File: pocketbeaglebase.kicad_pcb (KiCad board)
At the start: 2 copper layers, 100 x 60 mm, 87 parts, among them J1 RJ45-TRANSFO-2, P1 USB_2.0_Connector, P2 DSUB-9, P3 CONN_01X04, P4 CONN_02X20, P5 CONN_01X04, P6 CONN_01X04, P7 CONN_01X04, P8 CONN_02X03, P9 WR-TBL_691322310002, U1 BEAGLE_PocketBeagle, U2 LAN9514, U3 MIC2026, U4 MAX3227, U5 93LC66, U6 TPS54335A, Y1 25MHz

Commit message: review and discussion done
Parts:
- added P10: CONN_01X03, CON_wuerth:WR-TBL_691322310003, F.Cu at (181.9, 59.1)
- added U7: SN65HVD232, SOIC:SOIJ-8_5.3x5.3mm_Pitch1.27mm, F.Cu at (167.1, 34.1)
- C22, C24, C26, C27, C28: footprint capacitors:TantalC_SizeS_EIA-3216 -> capacitors:C_0603
- P2: value DSUB-9 -> CONN_01X03; footprint mechanical-connectors:DSUB-9_Female_Horizontal_P2.77x2.84mm_EdgePinOffset7.70mm_Housed_MountingHolesOffset9.12mm -> CON_wuerth:WR-TBL_691322310003
- moved P2 13.2 mm to (181.9, 74.0)
- moved C1 1.66 mm to (150.7, 80.5)
- moved C22 1.59 mm to (104.3, 62.8), turned to 270 degrees
- moved Y1 1.06 mm to (154.9, 80.0)
- moved C2 0.96 mm to (159.8, 80.0)
- moved C27 0.89 mm to (109.2, 60.1), turned to 0 degrees
- moved R2 0.75 mm to (155.6, 76.0)
- moved C28 0.64 mm to (109.8, 69.9), turned to 0 degrees
- moved C24 0.59 mm to (116.3, 64.6), turned to 90 degrees
- moved C26 0.56 mm to (104.3, 66.2), turned to 270 degrees
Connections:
- P2 pad 1: (no net) -> Net-(P2-Pad1)
- P2 pad 3: Net-(P2-Pad3) -> GND
- P4 pad 29: SCL2 -> (no net)
- P4 pad 31: SDA2 -> (no net)
- R21 pad 2: SDA2 -> (no net)
- R22 pad 2: SCL2 -> (no net)
- U1 pad 26: SDA2 -> (no net)
- U1 pad 28: SCL2 -> (no net)
- U4 pad 13: Net-(P2-Pad2) -> Net-(P2-Pad1)
- U4 pad 8: Net-(P2-Pad3) -> Net-(P2-Pad2)
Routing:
- net (no net): track 0.00 -> 108.8 mm, vias 0 -> 2
- net Net-(P2-Pad1): track 0.00 -> 87.4 mm, vias 0 -> 1
- net Net-(P2-Pad3): track 81.8 -> 0.00 mm, vias 1 -> 0
- net SDA2: track 56.2 -> 0.00 mm, vias 1 -> 0
- net SCL2: track 52.5 -> 0.00 mm, vias 1 -> 0
- net Net-(P2-Pad2): track 78.8 -> 91.3 mm
- net Net-(J1-Pad12): track 82.6 -> 87.1 mm
- net Net-(J1-Pad14): track 74.6 -> 79.0 mm
- net /LAN9514/nPWR2: track 56.6 -> 58.9 mm
- net Net-(C22-Pad1): track 5.05 -> 3.01 mm
- net GND: track 63.0 -> 64.4 mm, vias 16 -> 36
- net Net-(C1-Pad1): track 14.4 -> 15.7 mm
- net USB_DP: track 52.8 -> 51.6 mm
- net USB_DM: track 47.4 -> 46.2 mm
- net /LAN9514/nEEDO: track 10.8 -> 11.8 mm
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
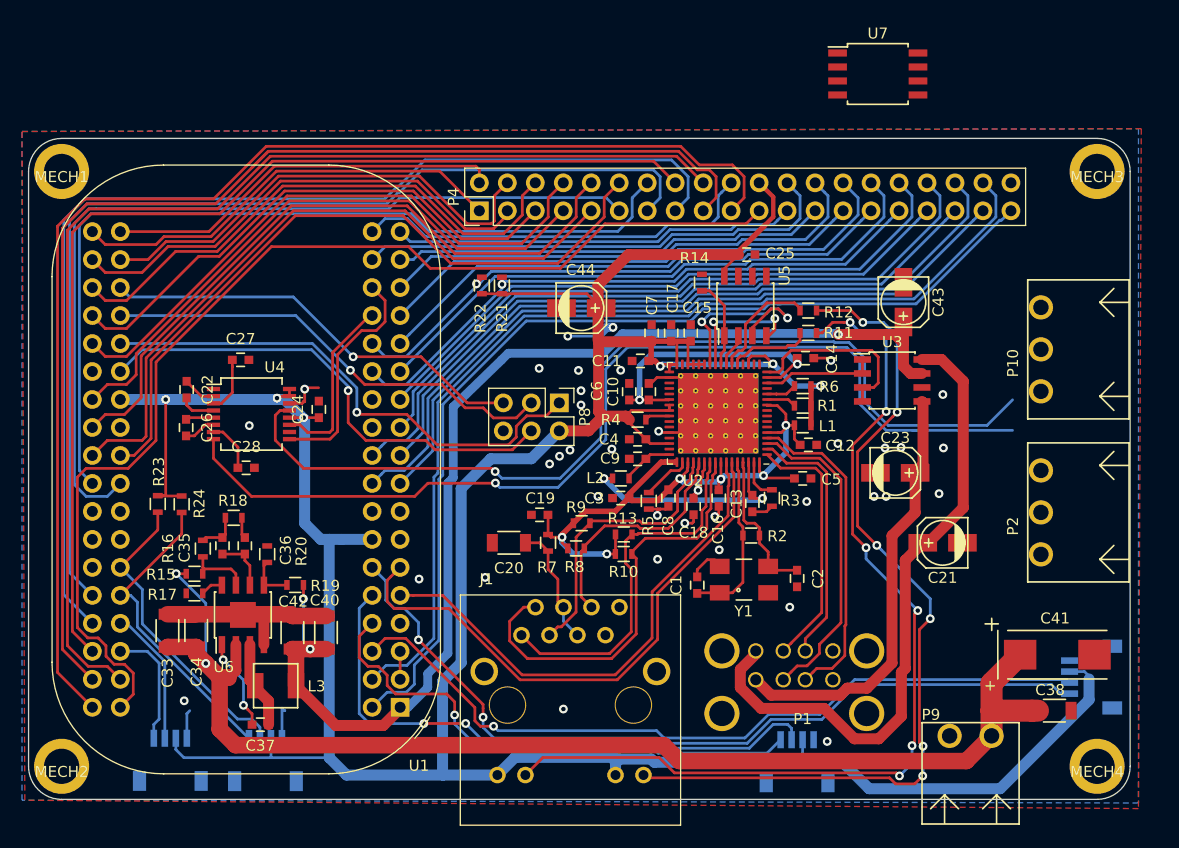
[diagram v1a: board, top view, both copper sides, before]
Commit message: added can bus
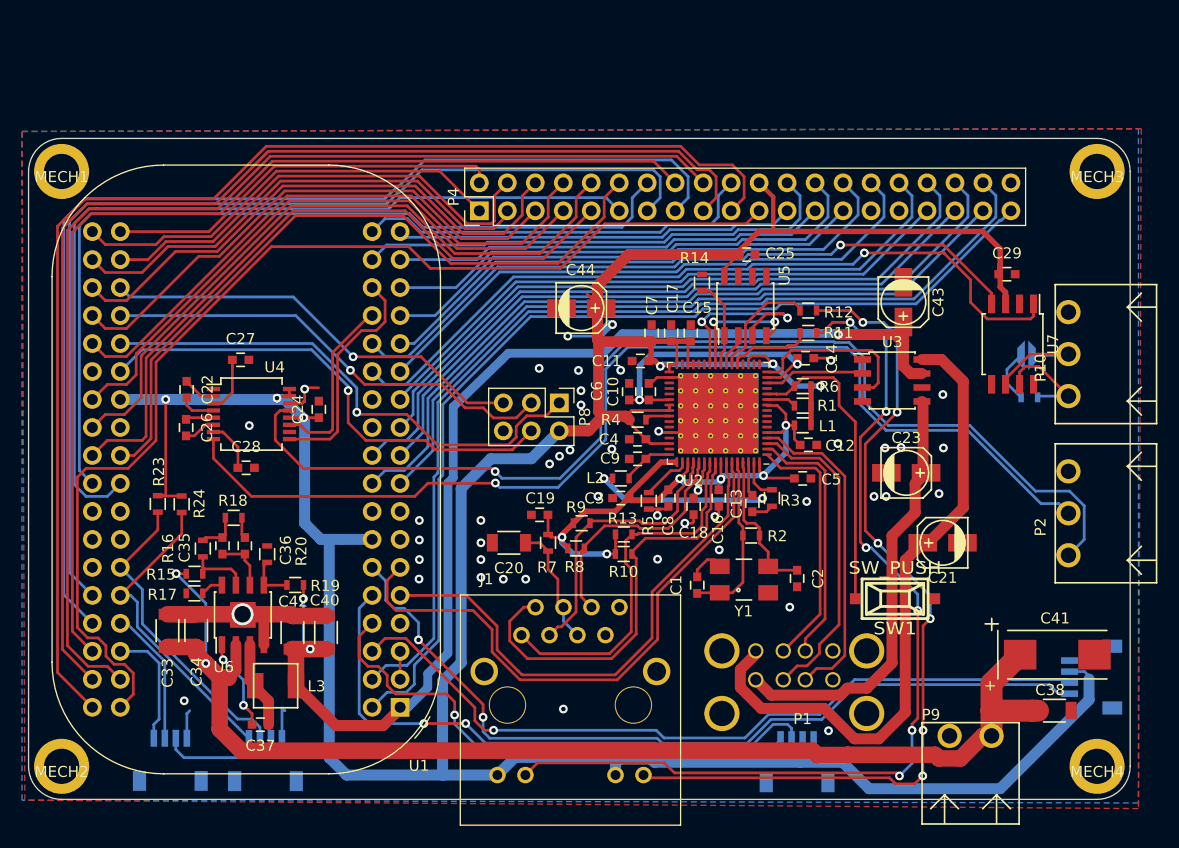
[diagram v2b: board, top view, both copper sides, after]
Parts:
- removed R22: 10k, resistors:R_0603
- added C29: 100nF, capacitors:C_0603, F.Cu at (178.8, 52.3)
- added P11: CONN_01X02, wire_pads:SolderJumper_2mm, B.Cu at (180.6, 59.7)
- added SW1: SW_PUSH, mechanical-switches:smd_push, F.Cu at (168.7, 81.8)
- P9: value WR-TBL_691322310002 -> WR-TBL_ 691322310002
- R21: value 10k -> 120R; moved to B.Cu
- moved R21 48.9 mm to (180.8, 63.5), turned to 0 degrees
- moved U7 27.4 mm to (179.3, 58.7), turned to 270 degrees
- moved P10 2.54 mm to (184.4, 59.6)
- moved P2 2.50 mm to (184.4, 74.0)
- moved C23 0.99 mm to (169.7, 70.4)
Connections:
- net Net-(P10-Pad2) renamed /UART/nCANL
- P10 pad 1: Net-(P10-Pad1) -> /UART/nCANH
- R21 pad 1: +3V3 -> Net-(P11-Pad1)
- R21 pad 2: (no net) -> /UART/nCANH
- U1 pad 26: (no net) -> CAN0_TX
- U1 pad 28: (no net) -> CAN0_RX
- U7 pad 1: (no net) -> CAN0_TX
- U7 pad 2: (no net) -> GND
- U7 pad 3: (no net) -> +3V3
- U7 pad 4: (no net) -> CAN0_RX
- U7 pad 7: Net-(P10-Pad1) -> /UART/nCANH
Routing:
- net (no net): track 108.8 -> 0.00 mm, vias 2 -> 0
- net CAN0_TX: track 0.00 -> 70.4 mm, vias 0 -> 1
- net CAN0_RX: track 0.00 -> 63.7 mm, vias 0 -> 1
- net Net-(R6-Pad1): track 2.79 -> 27.5 mm
- net +3V3: track 315.6 -> 333.8 mm
- net Net-(P2-Pad1): track 87.4 -> 101.0 mm
- net /UART/nCANL: track 0.00 -> 10.5 mm
- net /UART/nCANH: track 0.00 -> 9.71 mm
- net Net-(P2-Pad2): track 91.3 -> 99.4 mm
- net Net-(P11-Pad1): track 0.00 -> 4.88 mm
- net USB_DM: track 46.2 -> 47.5 mm
- net USB_DP: track 51.6 -> 52.8 mm
- net Net-(J1-Pad14): track 79.0 -> 78.1 mm
- net Net-(J1-Pad12): track 87.1 -> 86.4 mm
- net /LAN9514/nEEDI: track 18.0 -> 17.3 mm
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
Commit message: somehow done with general layouting
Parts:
- added D1: TVS, diodes:DO-214AB, F.Cu at (183.5, 86.7)
- P9: value WR-TBL_ 691322310002 -> WR-TBL_691322310002
- moved C38 77.4 mm to (105.7, 91.3), turned to 180 degrees
- moved C41 75.9 mm to (108.0, 95.9), turned to 180 degrees
- moved C21 5.40 mm to (177.0, 73.2)
- moved P6 2.29 mm to (186.4, 86.6)
- moved P7 1.91 mm to (113.4, 96.4)
- moved SW1 1.42 mm to (168.8, 80.4)
- moved P5 0.81 mm to (103.7, 96.4)
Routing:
- net GND: track 64.4 -> 85.2 mm, vias 45 -> 107
- net +BATT: track 110.0 -> 107.3 mm
- net +3V3: track 333.8 -> 331.2 mm
- net SCL1: track 28.2 -> 30.5 mm
- net Net-(J1-Pad14): track 78.1 -> 76.1 mm, vias 6 -> 4
- net SDA1: track 28.0 -> 29.9 mm
- net RX2: track 47.7 -> 46.0 mm
- net PR1_TX: track 70.6 -> 72.1 mm
- net Net-(R6-Pad1): track 27.5 -> 26.2 mm
- net Net-(J1-Pad12): track 86.4 -> 85.4 mm, vias 6 -> 4
- net PR1_RX: track 75.8 -> 76.6 mm

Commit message: finally
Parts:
- added L4: Label, labels:jecc_logo_7.2x2.2, F.Cu at (101.9, 43.4)
- added L5: Label, labels:Bot, F.Cu at (186.2, 48.5)
- added L6: Label, labels:Top, F.Cu at (186.2, 48.5)
- Y1: footprint crystals:Crystal_SMD_0603_4Pads -> crystals:Crystal_SMD_5x3.2mm_4Pad
- moved Y1 0.33 mm to (155.2, 80.3), turned to 180 degrees
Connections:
- U1 pad 3: USB_VBUS -> (no net)
- U1 pad 7: (no net) -> USB_VBUS
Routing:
- net GND: track 85.2 -> 145.7 mm, vias 107 -> 135
- net +3V3: track 331.2 -> 329.3 mm
- net PR1_TX: track 72.1 -> 71.2 mm
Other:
- board text added: "+"
- board text added: "CAN"
- board text added: "CAN Termination"
- board text added: "Expansion Header"
- board text added: "Hub Reset"
- board text added: "I2C1"
- board text added: "PWR"
- board text added: "RS-232"
- board text added: "SPI"
- board text added: "UART PRU1"
- board text added: "UART2"
- board text added: "UART4"
- board text added: "pocketbeaglebase"
